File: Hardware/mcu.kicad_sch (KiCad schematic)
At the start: 1 part, among them U2 STM32L412KBUx

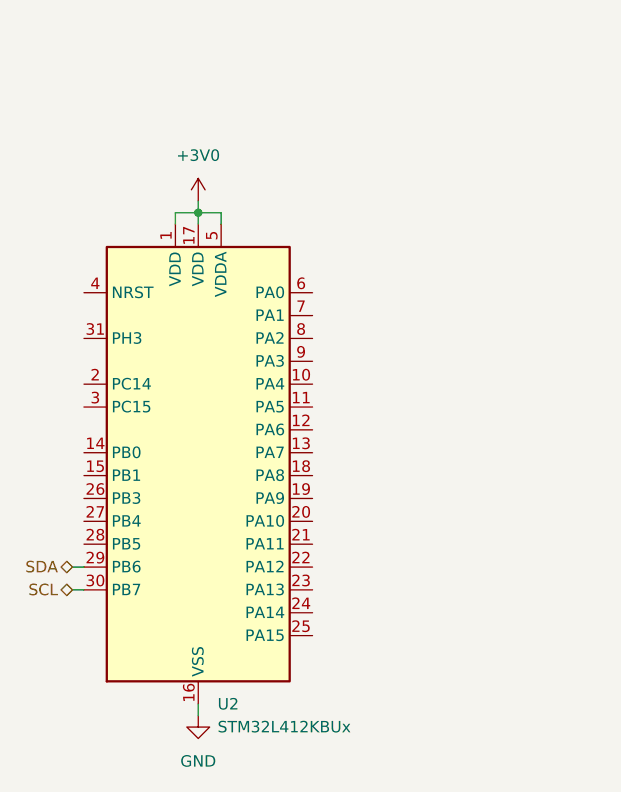
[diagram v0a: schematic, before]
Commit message: semi-final component placements and final component selections. Abandoning due to high routing complexity and need for a 4L board.
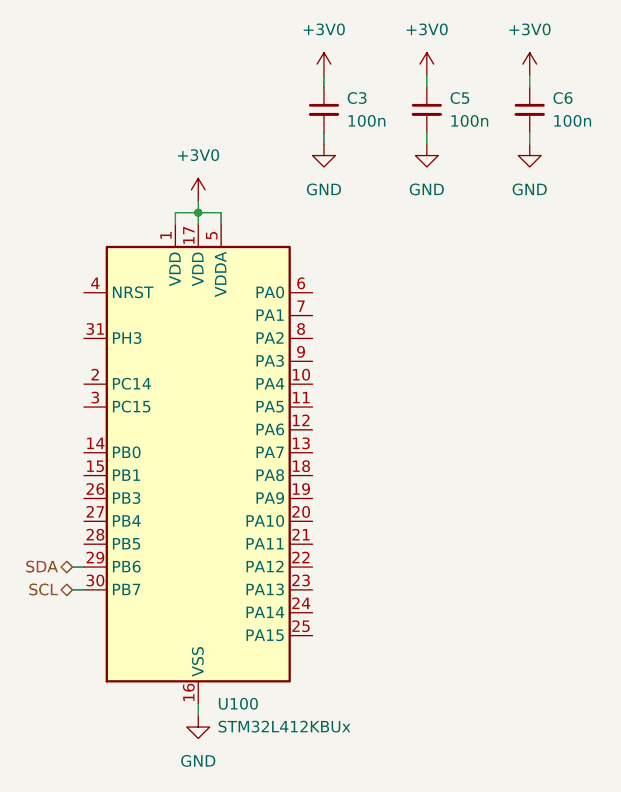
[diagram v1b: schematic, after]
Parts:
- added C3, C5, C6: 100n, LED_Custom:SMD_0402-2, symbol Device:C_Small
- renumbered U2 to U100
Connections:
- net +3V0: now also C3.1, C5.1, C6.1
- net GND: now also C3.2, C5.2, C6.2
